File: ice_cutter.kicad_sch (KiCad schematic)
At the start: 0 parts

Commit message: tracking datasheets, and schematic improvements
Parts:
- added C? (x2): C_Polarized_Small_US, symbol Device:C_Polarized_Small_US
- added C?: 100n, symbol Device:C_Small
- added C? (x2): 100n, Capacitor_SMD:C_0402_1005Metric, symbol Device:C_Small
- added C?: 10u, Capacitor_SMD:C_0603_1608Metric, symbol Device:C_Small
- added C?: C_Small, symbol Device:C_Small
- added D? (x2): LED_Small, symbol Device:LED_Small
- added D? (x2): D_Zener_Small, symbol Device:D_Zener_Small
- added J? (x2): Conn_01x01_Male, symbol Connector:Conn_01x01_Male
- added J?: Conn_01x03_Male, symbol Connector:Conn_01x03_Male
- added J?: Barrel_Jack, symbol Connector:Barrel_Jack
- added J?: Conn_02x03_Odd_Even, MyLibs:TC2030NL, symbol Connector_Generic:Conn_02x03_Odd_Even
- added Q? (x2): Q_NMOS_GSD, symbol Device:Q_NMOS_GSD
- added Q? (x2): Q_NPN_EBC, symbol Device:Q_NPN_EBC
- added Q?: Q_PNP_EBC, symbol Device:Q_PNP_EBC
- added R? (x7): R_Small_US, symbol Device:R_Small_US
- added R? (x3): 2k2, symbol Device:R_Small_US
- added R? (x2): 1k2, symbol Device:R_Small_US
- added SW? (x3): SW_Push, symbol Switch:SW_Push
- added TP? (x3): TestPoint, TestPoint:TestPoint_Pad_D2.0mm, symbol Connector:TestPoint
- added U?: SHT30-DIS, Sensor_Humidity:Sensirion_DFN-8-1EP_2.5x2.5mm_P0.5mm_EP1.1x1.7mm, symbol Sensor_Humidity:SHT30-DIS
- added U? (x6): MAN74A, Display_7Segment:MAN71A, symbol Display_Character:MAN74A
- added U?: LM317_TO-220, Package_TO_SOT_THT:TO-220-3_Vertical, symbol Regulator_Linear:LM317_TO-220
- added U?: LM7805_TO220, Package_TO_SOT_THT:TO-220-3_Vertical, symbol Regulator_Linear:LM7805_TO220
- added U?: L7812, symbol Regulator_Linear:L7812
- added U?: INA219AxD, Package_SO:SOIC-8_3.9x4.9mm_P1.27mm, symbol Analog_ADC:INA219AxD
- added U?: STM32G030XX, Package_SO:TSSOP-20_4.4x6.5mm_P0.65mm, symbol MyDevices:STM32G030XX
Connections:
- new net: D?.1 (K), Q?.1 (G), R?.1
- new net: U?.8 (VSS), U?.9 (VSS)
- new net: Q?.3 (C), R?.1
- new net: Q?.2 (B), R?.2 (x3)
- new net: D?.2 (A), R?.2 (x2)
- new net: Q?.3 (C), Q?.3 (C), R?.1
- new net: D?.1 (K), Q?.1 (G), R?.2
- new net +12V: Q?.1 (E)
- new net +3V3: C?.1, C?.1, C?.1, C?.1, J?.1 (Pin_1), J?.1 (Pin_1), R?.2, R?.2, R?.2, U?.4 (VDD), U?.5 (VS)
- new net Drive_FET_High: R?.1
- new net Drive_FET_Low: R?.1
- new net GND: C?.2, C?.2, C?.2, C?.2, D?.1 (K), D?.1 (K), D?.2 (A), D?.2 (A), J?.2, J?.3 (Pin_3), J?.5 (Pin_5), Q?.1 (E), Q?.1 (E), Q?.2 (S), Q?.2 (S), SW?.2, SW?.2, SW?.2, U?.5 (VSS), U?.6 (GND)
- new net LED1: R?.1, U?.2 (PB9/PC14-OSC32_IN)
- new net LED2: R?.1, U?.3 (PC15-OSC32_OUT)
- new net MCU_In: TP?.1, U?.10 (PA3)
- new net MCU_Out: TP?.1, U?.9 (PA2)
- new net NRST: J?.3 (Pin_3), SW?.1, U?.6 (NRST)
- new net PB1: SW?.1, U?.8 (PA1)
- new net PB2: SW?.1, U?.7 (PA0)
- new net SCL: R?.1, U?.16 (PA11[PA9]), U?.4 (SCL)
- new net SDA: R?.1, U?.17 (PA12[PA10]), U?.3 (SDA)
- new net SWCLK: J?.4 (Pin_4), U?.19 (PA15/PA14-BOOT0)
- new net SWDIO: J?.2 (Pin_2), U?.18 (PA13)
- new net VDC: J?.1, R?.1, U?.8 (IN+)
- new net VOUT_FAULT: Q?.3 (D), R?.1, TP?.1, U?.11 (PA4)
- new net Wire_H: J?.1 (Pin_1), R?.2, R?.2, R?.2, U?.7 (IN-)
- new net Wire_L: J?.1 (Pin_1), Q?.3 (D), R?.1
- new net pot: J?.2 (Pin_2)
- no-connect marks 0 -> 1
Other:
- note added: "7 Seg C252199"
- note added: "HMI"
- note added: "Input Power"
- note added: "LMT70 C110286"
- note added: "MCU"
- note added: "Needs work. Need a nice symbol and footprint for 7 seg and TM1620"
- note added: "Programming"
- note added: "Regulation"
- note added: "Resistor in parallel for normal operation and testing"
- note added: "Some DC input voltage preferably in the range of 15V - 20V"
- note added: "TM1620 C19579"
- note added: "TMP 117 C2803242"
- note added: "Wire Cutter"
- note added: "Wire Element"

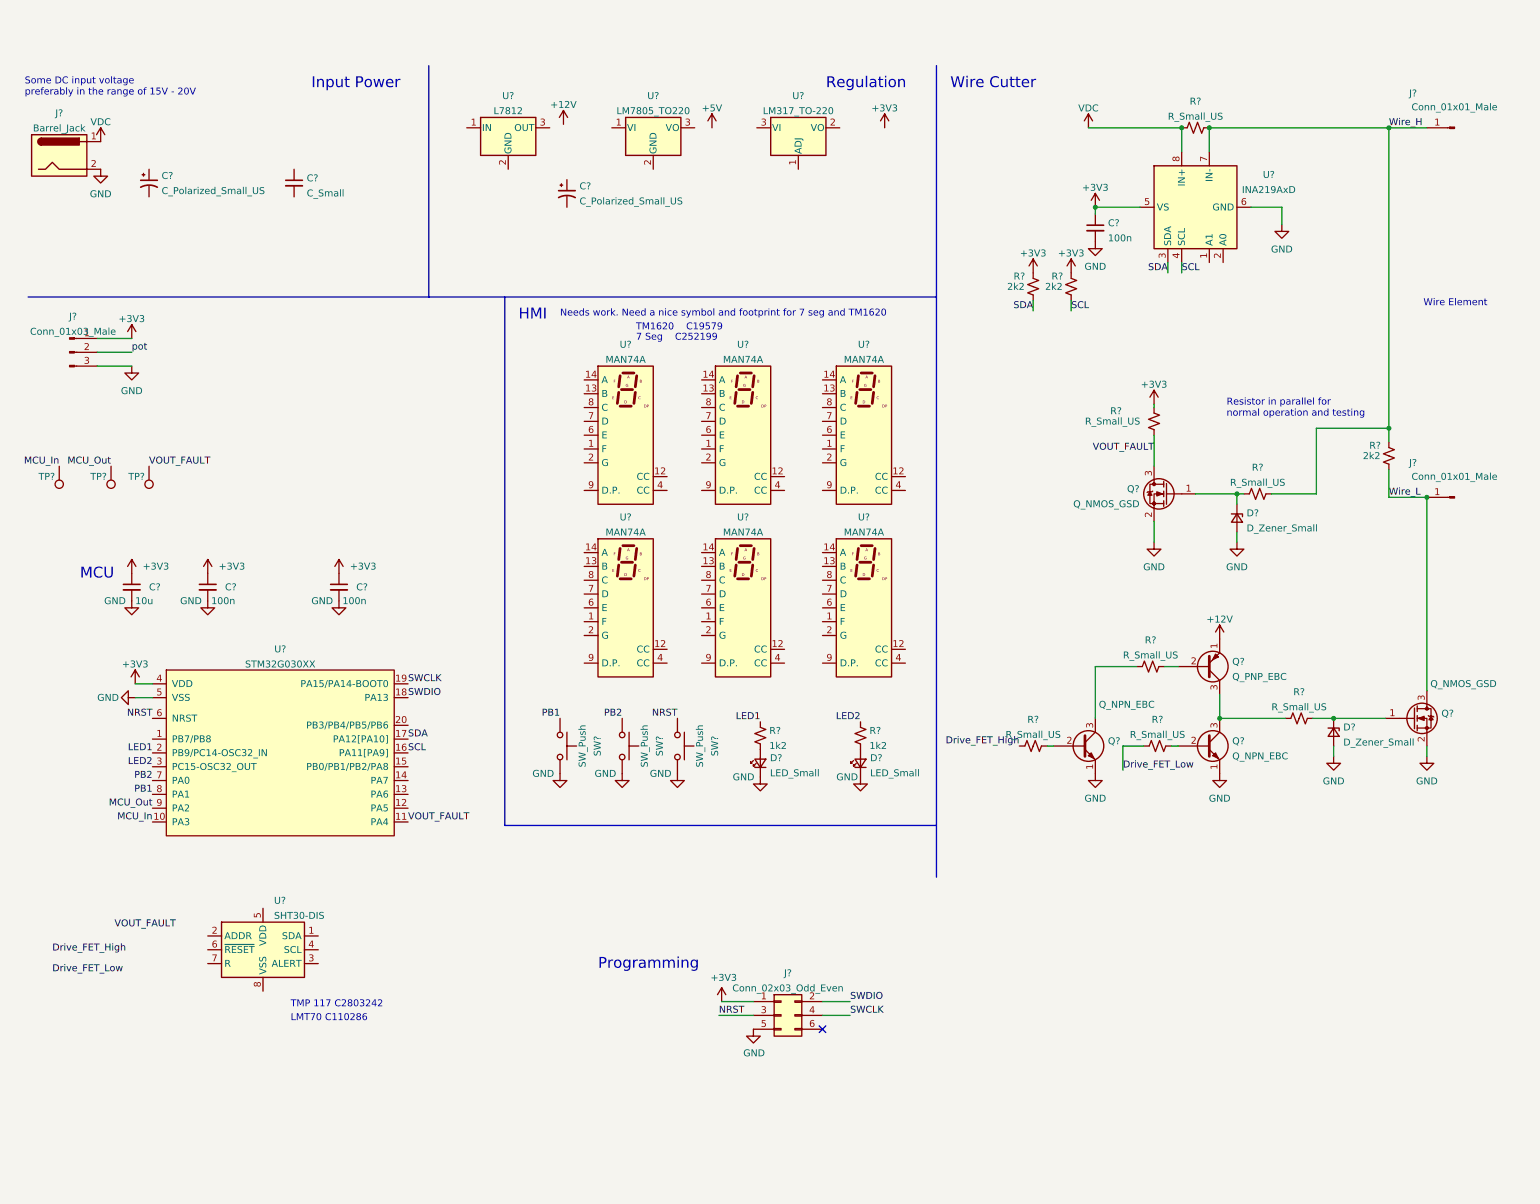
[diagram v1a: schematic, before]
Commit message: inclusion of motors and schematic improvements
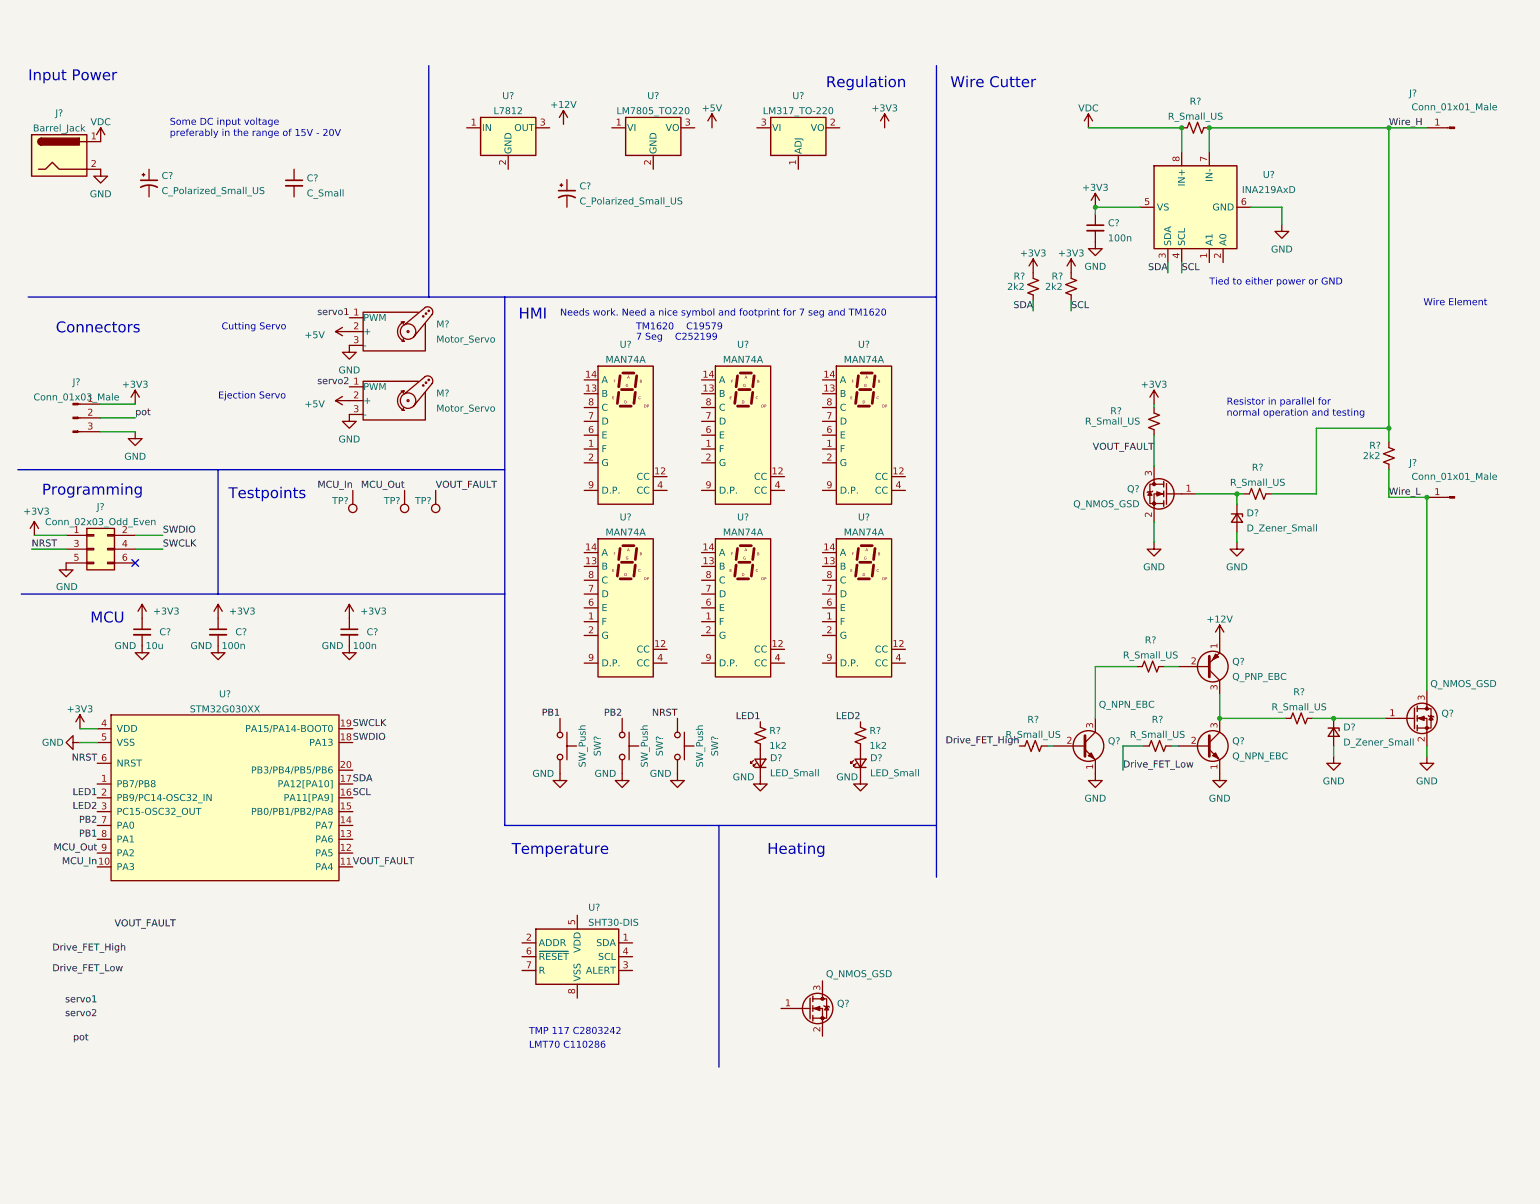
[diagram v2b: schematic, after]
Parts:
- added M? (x2): Motor_Servo, symbol Motor:Motor_Servo
- added Q?: Q_NMOS_GSD, symbol Device:Q_NMOS_GSD
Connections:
- net +5V: now also M?.2 (+), M?.2 (+)
- net GND: now also M?.3 (-), M?.3 (-)
- new net servo1: M?.1 (PWM)
- new net servo2: M?.1 (PWM)
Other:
- note added: "Connectors"
- note added: "Cutting Servo"
- note added: "Ejection Servo"
- note added: "Heating"
- note added: "Temperature"
- note added: "Testpoints"
- note added: "Tied to either power or GND"
- moved on the sheet: C?, J?, TP?, U?

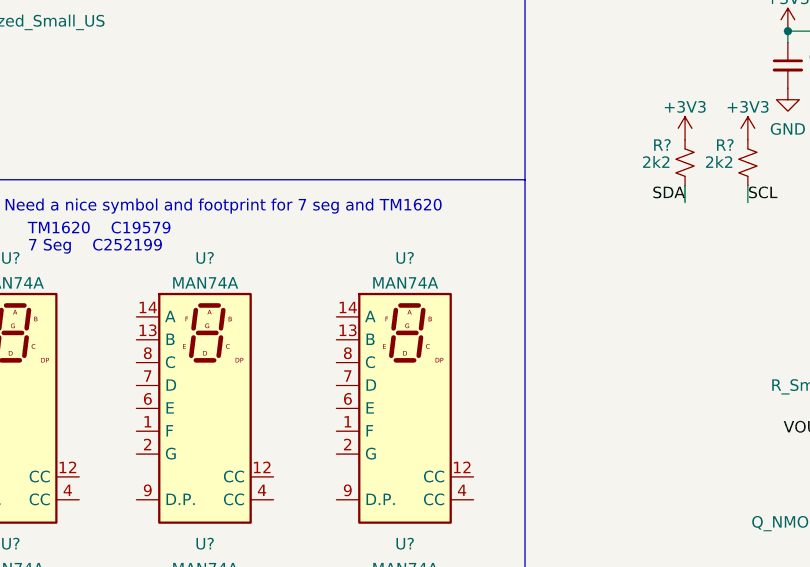
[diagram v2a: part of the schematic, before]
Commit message: Added TM1620 symbol to library(LED drive control)
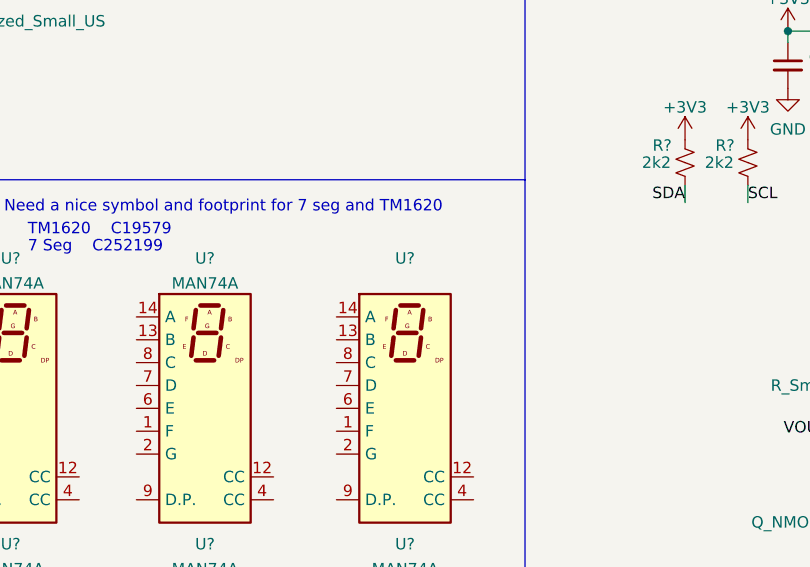
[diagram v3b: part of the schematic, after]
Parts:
- U?: value MAN74A -> (none); footprint Display_7Segment:MAN71A -> (none)
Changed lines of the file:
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@@
     (in_bom yes) (on_board yes) (fields_autoplaced)
     (property "Reference" "U?" (id 0) (at 167.64 64.6135 0))
-    (property "Value" "MAN74A" (id 1) (at 167.64 67.3886 0))
-    (property "Footprint" "Display_7Segment:MAN71A" (id 2) (at 154.94 99.06 0)
+    (property "Value" "" (id 1) (at 167.64 67.3886 0))
+    (property "Footprint" "" (id 2) (at 154.94 99.06 0)
       (effects (font (size 1.27 1.27)) (justify left) hide)
     )
